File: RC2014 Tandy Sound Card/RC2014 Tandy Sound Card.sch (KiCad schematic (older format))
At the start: 14 parts, among them J1 CONN_01X39, J2 Line Out, J3 Speaker Out, U1 74LS138, U2 74LS245, U3 SN76489AN, U4 TDA7056A

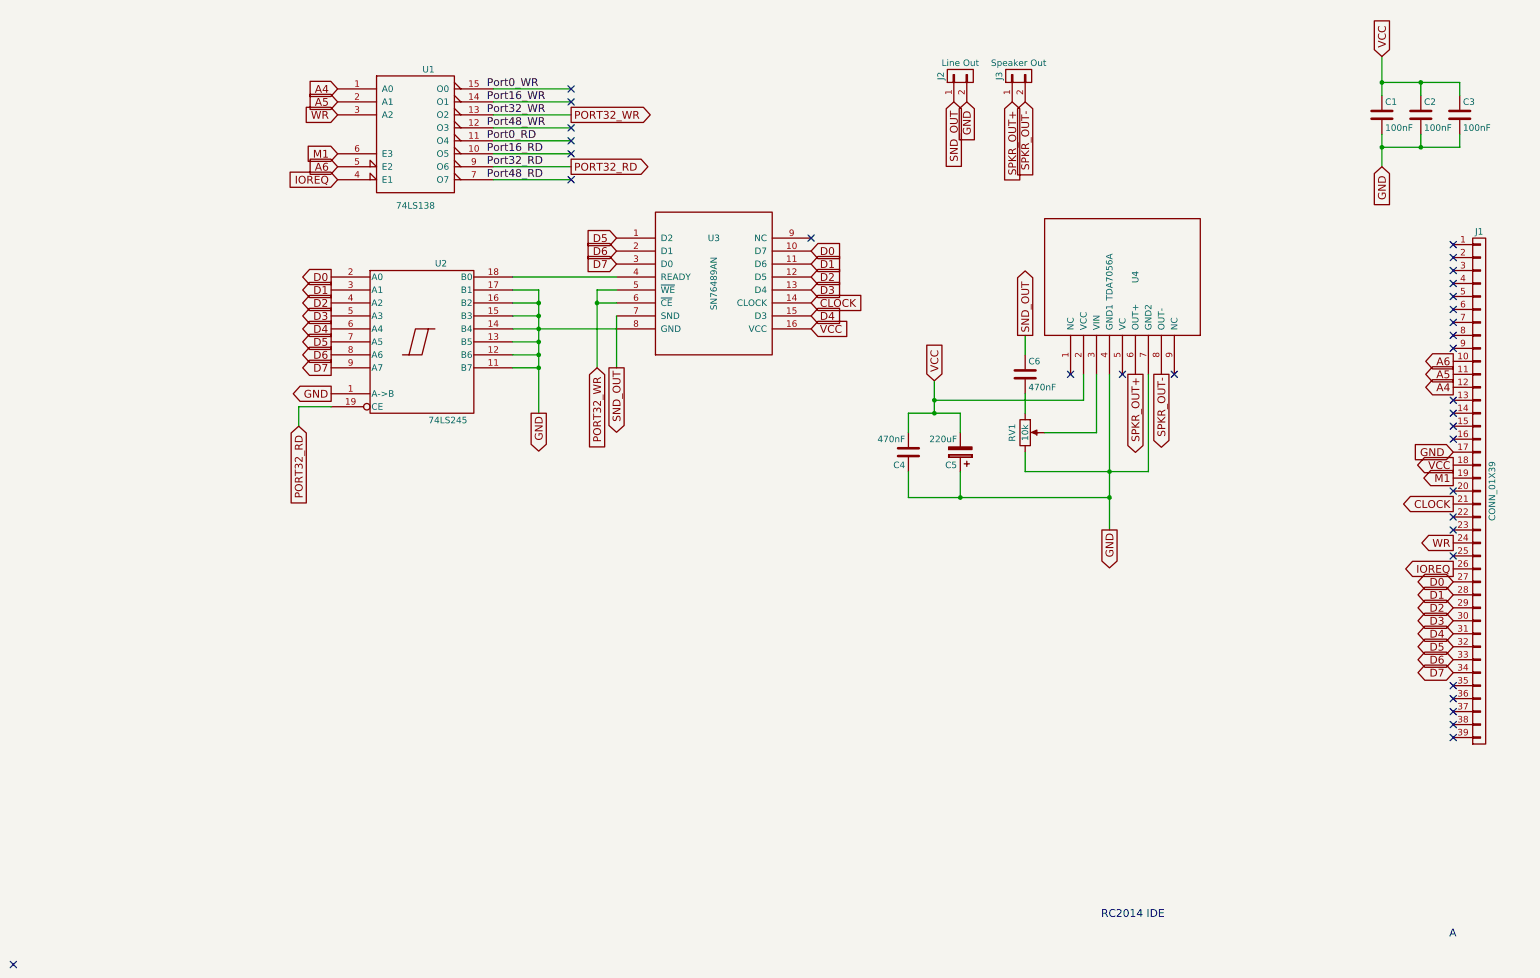
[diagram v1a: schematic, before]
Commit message: Added pinheaders for selecting address
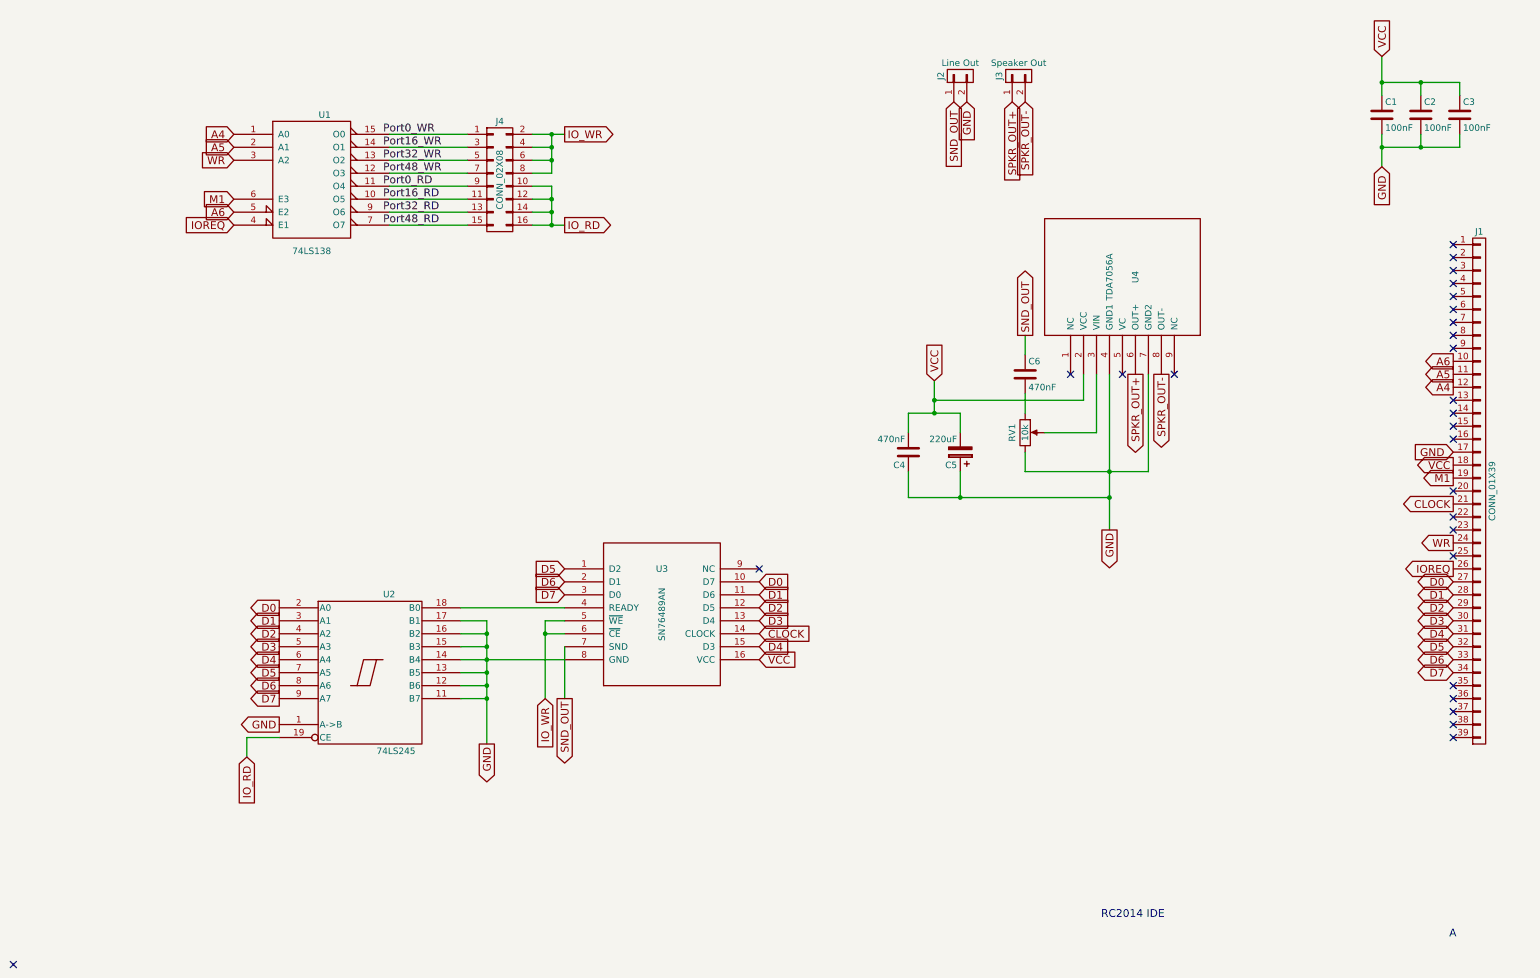
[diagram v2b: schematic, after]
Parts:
- added J4: CONN_02X08, Pin_Headers:Pin_Header_Straight_2x08_Pitch2.54mm, symbol CONN_02X08
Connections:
- net at U1.10 (O5): now also J4.11 (P11)
- net at U1.11 (O4): now also J4.9 (P9)
- net at U1.12 (O3): now also J4.7 (P7)
- net at U1.14 (O1): now also J4.3 (P3)
- net at U1.15 (O0): now also J4.1 (P1)
- net at U1.7 (O7): now also J4.15 (P15)
- net PORT32_RD: no longer names the net of U1.9 (O6)
- net PORT32_RD: now also J4.13 (P13); no longer U2.19 (CE)
- net PORT32_WR renamed IO_WR
- net IO_WR: now also J4.2 (P2), J4.4 (P4), J4.6 (P6), J4.8 (P8); no longer U1.13 (O2)
- new net: J4.5 (P5), U1.13 (O2)
- new net IO_RD: J4.10 (P10), J4.12 (P12), J4.14 (P14), J4.16 (P16), U2.19 (CE)
- no-connect marks 33 -> 27
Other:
- moved on the sheet: U1, U2, U3
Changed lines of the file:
@@
 $EndComp
 NoConn ~ 10600 6000
-Text GLabel 2000 1100 0    60   Input ~ 0
+Text GLabel 1200 1450 0    60   Input ~ 0
 A4
-Text GLabel 2000 1200 0    60   Input ~ 0
+Text GLabel 1200 1550 0    60   Input ~ 0
 A5
-Text GLabel 2000 1700 0    60   Input ~ 0
+Text GLabel 1200 2050 0    60   Input ~ 0
 A6
 Text GLabel 10600 4100 0    60   Output ~ 0
 M1
-Text GLabel 2000 1600 0    60   Input ~ 0
+Text GLabel 1200 1950 0    60   Input ~ 0
 M1
 Text GLabel 10600 4800 0    60   Output ~ 0
 IOREQ
-Text GLabel 2000 1800 0    60   Input ~ 0
+Text GLabel 1200 2150 0    60   Input ~ 0
 IOREQ
-NoConn ~ 3800 1100
-NoConn ~ 3800 1200
-NoConn ~ 3800 1500
-NoConn ~ 3800 1600
-NoConn ~ 3800 1800
 NoConn ~ 10600 4500
 NoConn ~ 10600 3100
@@
 L 74LS138 U1
 U 1 1 5913CEF9
-P 2600 1450
-F 0 "U1" H 2700 1950 50  0000 C CNN
-F 1 "74LS138" H 2600 900 50  0000 C CNN
-F 2 "Housings_DIP:DIP-16_W7.62mm_Socket" H 2600 1450 50  0001 C CNN
-F 3 "" H 2600 1450 50  0001 C CNN
-	1    2600 1450
+P 1800 1800
+F 0 "U1" H 1900 2300 50  0000 C CNN
+F 1 "74LS138" H 1800 1250 50  0000 C CNN
+F 2 "Housings_DIP:DIP-16_W7.62mm_Socket" H 1800 1800 50  0001 C CNN
+F 3 "" H 1800 1800 50  0001 C CNN
+	1    1800 1800
 	1    0    0    -1
 $EndComp
@@
 L 74LS245 U2
 U 1 1 59173606
-P 2650 3050
-F 0 "U2" H 2750 3625 50  0000 L BNN
-F 1 "74LS245" H 2700 2475 50  0000 L TNN
-F 2 "Housings_DIP:DIP-20_W7.62mm_Socket" H 2650 3050 50  0001 C CNN
-F 3 "" H 2650 3050 50  0001 C CNN
-	1    2650 3050
+P 2250 5600
+F 0 "U2" H 2350 6175 50  0000 L BNN
+F 1 "74LS245" H 2300 5025 50  0000 L TNN
+F 2 "Housings_DIP:DIP-20_W7.62mm_Socket" H 2250 5600 50  0001 C CNN
+F 3 "" H 2250 5600 50  0001 C CNN
+	1    2250 5600
 	1    0    0    -1
 $EndComp
@@
 L SN76489AN U3
 U 1 1 59173320
-P 4900 2600
-F 0 "U3" H 4900 2950 50  0000 C CNN
-F 1 "SN76489AN" V 4900 2600 50  0000 C CNN
-F 2 "Housings_DIP:DIP-16_W7.62mm_Socket" H 4900 3250 50  0001 C CNN
-F 3 "DOCUMENTATION" H 4900 1950 50  0001 C CNN
-	1    4900 2600
-	1    0    0    -1
-$EndComp
-Text GLabel 1950 3450 0    60   Output ~ 0
+P 4500 5150
+F 0 "U3" H 4500 5500 50  0000 C CNN
+F 1 "SN76489AN" V 4500 5150 50  0000 C CNN
+F 2 "Housings_DIP:DIP-16_W7.62mm_Socket" H 4500 5800 50  0001 C CNN
+F 3 "DOCUMENTATION" H 4500 4500 50  0001 C CNN
+	1    4500 5150
+	1    0    0    -1
+$EndComp
+Text GLabel 1550 6000 0    60   Output ~ 0
 GND
-Text GLabel 3550 3600 3    60   Output ~ 0
+Text GLabel 3150 6150 3    60   Output ~ 0
 GND
-Text GLabel 1950 2550 0    60   Output ~ 0
+Text GLabel 1550 5100 0    60   Output ~ 0
 D0
-Text GLabel 1950 2650 0    60   Output ~ 0
+Text GLabel 1550 5200 0    60   Output ~ 0
 D1
-Text GLabel 1950 2750 0    60   Output ~ 0
+Text GLabel 1550 5300 0    60   Output ~ 0
 D2
-Text GLabel 1950 2850 0    60   Output ~ 0
+Text GLabel 1550 5400 0    60   Output ~ 0
 D3
-Text GLabel 1950 2950 0    60   Output ~ 0
+Text GLabel 1550 5500 0    60   Output ~ 0
 D4
-Text GLabel 1950 3050 0    60   Output ~ 0
+Text GLabel 1550 5600 0    60   Output ~ 0
 D5
-Text GLabel 1950 3150 0    60   Output ~ 0
+Text GLabel 1550 5700 0    60   Output ~ 0
 D6
-Text GLabel 1950 3250 0    60   Output ~ 0
+Text GLabel 1550 5800 0    60   Output ~ 0
 D7
-Text GLabel 5650 2350 2    60   Input ~ 0
+Text GLabel 5250 4900 2    60   Input ~ 0
 D0
-Text GLabel 5650 2450 2    60   Input ~ 0
+Text GLabel 5250 5000 2    60   Input ~ 0
 D1
-Text GLabel 5650 2550 2    60   Input ~ 0
+Text GLabel 5250 5100 2    60   Input ~ 0
 D2
-Text GLabel 5650 2650 2    60   Input ~ 0
+Text GLabel 5250 5200 2    60   Input ~ 0
 D3
-Text GLabel 5650 2850 2    60   Input ~ 0
+Text GLabel 5250 5400 2    60   Input ~ 0
 D4
-Text GLabel 4150 2250 0    60   Input ~ 0
+Text GLabel 3750 4800 0    60   Input ~ 0
 D5
-Text GLabel 4150 2350 0    60   Input ~ 0
+Text GLabel 3750 4900 0    60   Input ~ 0
 D6
-Text GLabel 4150 2450 0    60   Input ~ 0
+Text GLabel 3750 5000 0    60   Input ~ 0
 D7
-Text GLabel 5650 2950 2    60   Input ~ 0
+Text GLabel 5250 5500 2    60   Input ~ 0
 VCC
-NoConn ~ 5650 2250
-Text GLabel 2000 1300 0    60   Input ~ 0
+NoConn ~ 5250 4800
+Text GLabel 1200 1650 0    60   Input ~ 0
 WR
-NoConn ~ 3800 1400
-Text Label 3150 1500 0    60   ~ 0
+Text Label 2350 1850 0    60   ~ 0
 Port0_RD
-Text Label 3150 1100 0    60   ~ 0
+Text Label 2350 1450 0    60   ~ 0
 Port0_WR
-Text Label 3150 1200 0    60   ~ 0
+Text Label 2350 1550 0    60   ~ 0
 Port16_WR
-Text Label 3150 1300 0    60   ~ 0
+Text Label 2350 1650 0    60   ~ 0
 Port32_WR
-Text Label 3150 1400 0    60   ~ 0
+Text Label 2350 1750 0    60   ~ 0
 Port48_WR
-Text Label 3150 1600 0    60   ~ 0
+Text Label 2350 1950 0    60   ~ 0
 Port16_RD
-Text Label 3150 1700 0    60   ~ 0
+Text Label 2350 2050 0    60   ~ 0
 Port32_RD
-Text Label 3150 1800 0    60   ~ 0
+Text Label 2350 2150 0    60   ~ 0
 Port48_RD
 Text GLabel 10600 4300 0    60   Output ~ 0
 CLOCK
-Text GLabel 5650 2750 2    60   Input ~ 0
+Text GLabel 5250 5300 2    60   Input ~ 0
 CLOCK
-Text GLabel 3800 1700 2    60   Output ~ 0
-PORT32_RD
-Text GLabel 3800 1300 2    60   Output ~ 0
-PORT32_WR
-Text GLabel 4000 3250 3    60   Input ~ 0
-PORT32_WR
-Text GLabel 1700 3700 3    60   Input ~ 0
-PORT32_RD
-Text GLabel 4150 3250 3    60   Output ~ 0
+Text GLabel 3750 2150 2    60   Output ~ 0
+IO_RD
+Text GLabel 3750 1450 2    60   Output ~ 0
+IO_WR
+Text GLabel 3600 5800 3    60   Input ~ 0
+IO_WR
+Text GLabel 1300 6250 3    60   Input ~ 0
+IO_RD
+Text GLabel 3750 5800 3    60   Output ~ 0
 SND_OUT
 $Comp
@@
 	-1   0    0    1
 $EndComp
+NoConn ~ 8050 3300
+$Comp
+L CONN_02X08 J4
+U 1 1 591A29AB
+P 3250 1800
+F 0 "J4" H 3250 2250 50  0000 C CNN
+F 1 "CONN_02X08" V 3250 1800 50  0000 C CNN
+F 2 "Pin_Headers:Pin_Header_Straight_2x08_Pitch2.54mm" H 3250 600 50  0001 C CNN
+F 3 "" H 3250 600 50  0001 C CNN
+	1    3250 1800
+	1    0    0    -1
+$EndComp
 Wire Wire Line
 	10050 850  10050 1150
@@
 	10050 1450 10050 1700
 Wire Wire Line
-	3350 2550 4150 2550
-Wire Wire Line
-	3350 2650 3550 2650
-Wire Wire Line
-	3550 2650 3550 3600
-Wire Wire Line
-	3350 2750 3550 2750
-Connection ~ 3550 2750
-Wire Wire Line
-	3350 2850 3550 2850
-Connection ~ 3550 2850
-Wire Wire Line
-	3350 2950 4150 2950
-Connection ~ 3550 2950
-Wire Wire Line
-	3350 3050 3550 3050
-Connection ~ 3550 3050
-Wire Wire Line
-	3350 3150 3550 3150
-Connection ~ 3550 3150
-Wire Wire Line
-	3350 3250 3550 3250
-Connection ~ 3550 3250
-Wire Wire Line
-	3200 1400 3800 1400
-Wire Wire Line
-	3800 1300 3200 1300
-Wire Wire Line
-	3800 1200 3200 1200
-Wire Wire Line
-	3800 1500 3200 1500
-Wire Wire Line
-	3800 1600 3200 1600
-Wire Wire Line
-	3800 1700 3200 1700
-Wire Wire Line
-	3800 1800 3200 1800
-Wire Wire Line
-	3800 1100 3200 1100
-Wire Wire Line
-	1700 3700 1700 3550
-Wire Wire Line
-	1700 3550 1950 3550
-Wire Wire Line
-	4000 2650 4000 3250
-Wire Wire Line
-	4000 2650 4150 2650
-Wire Wire Line
-	4150 2750 4000 2750
-Connection ~ 4000 2750
-Wire Wire Line
-	4150 2850 4150 3250
+	2950 5100 3750 5100
+Wire Wire Line
+	2950 5200 3150 5200
+Wire Wire Line
+	3150 5200 3150 6150
+Wire Wire Line
+	2950 5300 3150 5300
+Connection ~ 3150 5300
+Wire Wire Line
+	2950 5400 3150 5400
+Connection ~ 3150 5400
+Wire Wire Line
+	2950 5500 3750 5500
+Connection ~ 3150 5500
+Wire Wire Line
+	2950 5600 3150 5600
+Connection ~ 3150 5600
+Wire Wire Line
+	2950 5700 3150 5700
+Connection ~ 3150 5700
+Wire Wire Line
+	2950 5800 3150 5800
+Connection ~ 3150 5800
+Wire Wire Line
+	3000 1450 2400 1450
+Wire Wire Line
+	1300 6250 1300 6100
+Wire Wire Line
+	1300 6100 1550 6100
+Wire Wire Line
+	3600 5200 3600 5800
+Wire Wire Line
+	3600 5200 3750 5200
+Wire Wire Line
+	3750 5300 3600 5300
+Connection ~ 3600 5300
+Wire Wire Line
+	3750 5400 3750 5800
 Wire Wire Line
 	10050 1050 10650 1050
@@
 Connection ~ 6600 3600
 Connection ~ 6600 3500
-NoConn ~ 8050 3300
+Wire Wire Line
+	2400 2050 3000 2050
+Wire Wire Line
+	2400 2150 3000 2150
+Wire Wire Line
+	2400 1950 3000 1950
+Wire Wire Line
+	2400 1850 3000 1850
+Wire Wire Line
+	2400 1750 3000 1750
+Wire Wire Line
+	2400 1650 3000 1650
+Wire Wire Line
+	2400 1550 3000 1550
+Wire Wire Line
+	3500 2150 3750 2150
+Wire Wire Line
+	3500 2050 3650 2050
+Wire Wire Line
+	3650 1850 3650 2150
+Connection ~ 3650 2150
+Wire Wire Line
+	3650 1950 3500 1950
+Connection ~ 3650 2050
+Wire Wire Line
+	3500 1850 3650 1850
+Connection ~ 3650 1950
+Wire Wire Line
+	3500 1450 3750 1450
+Wire Wire Line
+	3500 1750 3650 1750
+Wire Wire Line
+	3650 1750 3650 1450
+Connection ~ 3650 1450
+Wire Wire Line
+	3500 1650 3650 1650
+Connection ~ 3650 1650
+Wire Wire Line
+	3500 1550 3650 1550
+Connection ~ 3650 1550
 $EndSCHEMATC
